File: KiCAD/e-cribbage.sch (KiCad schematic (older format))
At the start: 559 parts, among them U1 74HC595D_118, U10 74HC595D_118, U11 74HC595D_118, U12 74HC595D_118, U13 74HC595D_118, U14 74HC595D_118, U15 74HC595D_118, U16 74HC595D_118, U17 74HC595D_118, U18 74HC595D_118, U19 74HC595D_118, U2 MSP430F2012IPW, U20 74HC595D_118, U21 74HC595D_118, U22 74HC595D_118, U23 74HC595D_118, U24 74HC595D_118, U25 74HC595D_118, U26 74HC595D_118, U27 74HC595D_118, U28 74HC595D_118, U29 74HC595D_118, U3 74HC595D_118, U30 74HC595D_118, U31 74HC595D_118, U32 SN74LVC1G08DBVR, U33 SN74LVC1G125DCKR, U4 74HC595D_118, U5 74HC595D_118, U6 74HC595D_118, U7 74HC595D_118, U8 74HC595D_118, U9 74HC595D_118

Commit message: reduced 0603 footprints
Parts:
- D100, D101, D102, D103, D104, D105, D106, D107, D108, D109, D11, D110, D111, D112, D113, D114, D115, D116, D117, D118, D119, D12, D120, D121, D122, D123, D124, D125, D126, D127, D128, D129, D13, D130, D131, D132, D133, D134, D135, D136, D137, D138, D139, D14, D140, D141, D142, D143, D144, D145, D146, D147, D148, D149, D15, D150, D151, D152, D153, D154, D155, D156, D157, D158, D159, D16, D160, D161, D162, D163, D164, D165, D166, D167, D168, D169, D17, D170, D171, D172, D173, D174, D175, D176, D177, D178, D179, D18, D180, D181, D182, D183, D184, D185, D186, D187, D188, D189, D19, D190, D191, D192, D193, D194, D195, D196, D197, D198, D199, D20, D200, D201, D202, D203, D204, D205, D206, D207, D208, D209, D21, D210, D211, D212, D213, D214, D215, D216, D217, D218, D219, D22, D220, D221, D222, D223, D224, D225, D226, D227, D228, D229, D23, D230, D231, D232, D233, D234, D235, D236, D237, D238, D239, D24, D240, D25, D26, D27, D28, D29, D30, D31, D32, D33, D34, D35, D36, D37, D38, D39, D40, D41, D42, D43, D44, D45, D46, D47, D48, D49, D50, D51, D52, D53, D54, D55, D56, D57, D58, D59, D60, D61, D62, D63, D64, D65, D66, D67, D68, D69, D70, D71, D72, D73, D74, D75, D76, D77, D78, D79, D80, D81, D82, D83, D84, D85, D86, D87, D88, D89, D90, D91, D92, D93, D94, D95, D96, D97, D98, D99: footprint LEDs:LED_0603_HandSoldering -> LEDs:LED_0603
- R100, R101, R102, R103, R104, R105, R106, R107, R108, R109, R11, R110, R111, R112, R113, R114, R115, R116, R117, R118, R119, R12, R120, R121, R122, R123, R124, R125, R126, R127, R128, R129, R13, R130, R131, R132, R133, R134, R135, R136, R137, R138, R139, R14, R140, R141, R142, R143, R144, R145, R146, R147, R148, R149, R15, R150, R151, R152, R153, R154, R155, R156, R157, R158, R159, R16, R160, R161, R162, R163, R164, R165, R166, R167, R168, R169, R17, R170, R171, R172, R173, R174, R175, R176, R177, R178, R179, R18, R180, R181, R182, R183, R184, R185, R186, R187, R188, R189, R19, R190, R191, R192, R193, R194, R195, R196, R197, R198, R199, R20, R200, R201, R202, R203, R204, R205, R206, R207, R208, R209, R21, R210, R211, R212, R213, R214, R215, R216, R217, R218, R219, R22, R220, R221, R222, R223, R224, R225, R226, R227, R228, R229, R23, R230, R231, R232, R233, R234, R235, R236, R237, R238, R239, R24, R240, R241, R242, R243, R244, R245, R246, R247, R248, R249, R25, R250, R26, R27, R28, R29, R30, R31, R32, R33, R34, R35, R36, R37, R38, R39, R40, R41, R42, R43, R44, R45, R46, R47, R48, R49, R50, R51, R52, R53, R54, R55, R56, R57, R58, R59, R60, R61, R62, R63, R64, R65, R66, R67, R68, R69, R70, R71, R72, R73, R74, R75, R76, R77, R78, R79, R80, R81, R82, R83, R84, R85, R86, R87, R88, R89, R90, R91, R92, R93, R94, R95, R96, R97, R98, R99: footprint Resistors_SMD:R_0603_HandSoldering -> Resistors_SMD:R_0603

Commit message: power and ground planes added 471 nets unconnected
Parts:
- added C32, C33, C34, C35: 1.0uF, Capacitors_SMD:C_0603_HandSoldering, symbol Device:C
- added R251: 47k, Resistors_SMD:R_0603, symbol Device:R
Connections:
- net labels added: RST, TEST
- wire segments 1708 -> 1768
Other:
- moved on the sheet: BAT1, C2, R243, R244, R246, R247, S1, S2, S3, S4, U2

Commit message: preliminary part placement and route
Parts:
- removed R241, R242, R245, R248, R249, R250: 10k, Resistors_SMD:R_0603, symbol Device:R
- removed U33: SN74LVC1G125DCKR, digikey-footprints:SOT-353, symbol dk_Logic-Buffers-Drivers-Receivers-Transceivers:SN74LVC1G125DCKR
- added C36, C37, C38, C39: 1.0uF, Capacitors_SMD:C_0603_HandSoldering, symbol Device:C
- added U34, U35, U36, U37, U38, U39, U40: SN74LVC1G08DBVR, digikey-footprints:SOT-753, symbol dk_Logic-Gates-and-Inverters:SN74LVC1G08DBVR
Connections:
- net labels added: CLK1A, CLK1B, CLK1C, CLK1D, CLK2A, CLK2B, CLK2C, CLK2D
- wire segments 1768 -> 1848
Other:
- moved on the sheet: BAT1, C2, C32, C33, C34, C35, R243, R244, R246, R247, R251, S1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

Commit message: clock fanout added to schematic
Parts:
- BAT1: symbol dk_Battery-Holders-Clips-Contacts:BS-7 -> e-cribbage-rescue:BS-7-dk_Battery-Holders-Clips-Contacts
- S1, S2, S3, S4: symbol dk_Pushbutton-Switches:GPTS203211B -> e-cribbage-rescue:GPTS203211B-dk_Pushbutton-Switches
- U1, U10, U11, U12, U13, U14, U15, U16, U17, U18, U19, U20, U21, U22, U23, U24, U25, U26, U27, U28, U29, U3, U30, U31, U4, U5, U6, U7, U8, U9: symbol dk_Logic-Shift-Registers:74HC595D_118 -> e-cribbage-rescue:74HC595D_118-dk_Logic-Shift-Registers
- U32, U34, U35, U36, U37, U38, U39, U40: symbol dk_Logic-Gates-and-Inverters:SN74LVC1G08DBVR -> e-cribbage-rescue:SN74LVC1G08DBVR-dk_Logic-Gates-and-Inverters
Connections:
- net +3V3: now also U10.10 (MR), U10.13 (OE), U11.10 (MR), U11.13 (OE), U12.10 (MR), U12.13 (OE), U13.10 (MR), U13.13 (OE), U14.10 (MR), U14.13 (OE), U17.10 (MR), U17.13 (OE), U18.10 (MR), U18.13 (OE), U19.10 (MR), U19.13 (OE), U20.10 (MR), U20.13 (OE), U21.10 (MR), U21.13 (OE), U22.10 (MR), U22.13 (OE), U23.10 (MR), U23.13 (OE), U24.10 (MR), U24.13 (OE), U25.10 (MR), U25.13 (OE), U26.10 (MR), U26.13 (OE), U27.10 (MR), U27.13 (OE), U28.10 (MR), U28.13 (OE), U29.10 (MR), U29.13 (OE), U30.10 (MR), U30.13 (OE), U31.10 (MR), U31.13 (OE), U5.10 (MR), U5.13 (OE), U6.10 (MR), U6.13 (OE), U7.10 (MR), U7.13 (OE), U8.10 (MR), U8.13 (OE), U9.10 (MR), U9.13 (OE)
- net CLK: no longer U17.11 (SHCP), U17.12 (STCP)
- net CLK1B: now also U6.11 (SHCP), U6.12 (STCP), U7.11 (SHCP), U7.12 (STCP), U8.11 (SHCP), U8.12 (STCP), U9.11 (SHCP), U9.12 (STCP)
- net CLK1C: now also U10.11 (SHCP), U10.12 (STCP), U11.11 (SHCP), U11.12 (STCP), U12.11 (SHCP), U12.12 (STCP), U13.11 (SHCP), U13.12 (STCP)
- net CLK1D: now also U14.11 (SHCP), U14.12 (STCP), U15.11 (SHCP), U15.12 (STCP), U16.11 (SHCP), U16.12 (STCP)
- net CLK2A: now also U17.11 (SHCP), U17.12 (STCP), U18.11 (SHCP), U18.12 (STCP), U19.11 (SHCP), U19.12 (STCP), U20.11 (SHCP), U20.12 (STCP)
- net CLK2B: now also U21.11 (SHCP), U21.12 (STCP), U22.11 (SHCP), U22.12 (STCP), U23.11 (SHCP), U23.12 (STCP), U24.11 (SHCP), U24.12 (STCP)
- net CLK2C: now also U26.11 (SHCP), U26.12 (STCP), U27.11 (SHCP), U27.12 (STCP), U28.11 (SHCP), U28.12 (STCP)
- net CLK2D: now also U29.11 (SHCP), U29.12 (STCP), U30.11 (SHCP), U30.12 (STCP), U31.11 (SHCP), U31.12 (STCP)
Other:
- moved on the sheet: C17, C18, C19, C20, C21, C22, C29, C30, C31, D121, D122, D123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

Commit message: OE pulled low
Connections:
- net +3V3: no longer U1.13 (OE), U10.13 (OE), U11.13 (OE), U12.13 (OE), U13.13 (OE), U14.13 (OE), U15.13 (OE), U16.13 (OE), U17.13 (OE), U18.13 (OE), U19.13 (OE), U20.13 (OE), U21.13 (OE), U22.13 (OE), U25.13 (OE), U26.13 (OE), U27.13 (OE), U28.13 (OE), U29.13 (OE), U3.13 (OE), U30.13 (OE), U31.13 (OE), U5.13 (OE), U6.13 (OE), U7.13 (OE), U8.13 (OE), U9.13 (OE)
- net CLK2C: now also U25.11 (SHCP), U25.12 (STCP)
- net GND: now also U1.13 (OE), U10.13 (OE), U11.13 (OE), U12.13 (OE), U13.13 (OE), U14.13 (OE), U15.13 (OE), U16.13 (OE), U17.13 (OE), U18.13 (OE), U19.13 (OE), U20.13 (OE), U21.13 (OE), U22.13 (OE), U25.13 (OE), U26.13 (OE), U27.13 (OE), U28.13 (OE), U29.13 (OE), U3.13 (OE), U30.13 (OE), U31.13 (OE), U5.13 (OE), U6.13 (OE), U7.13 (OE), U8.13 (OE), U9.13 (OE)

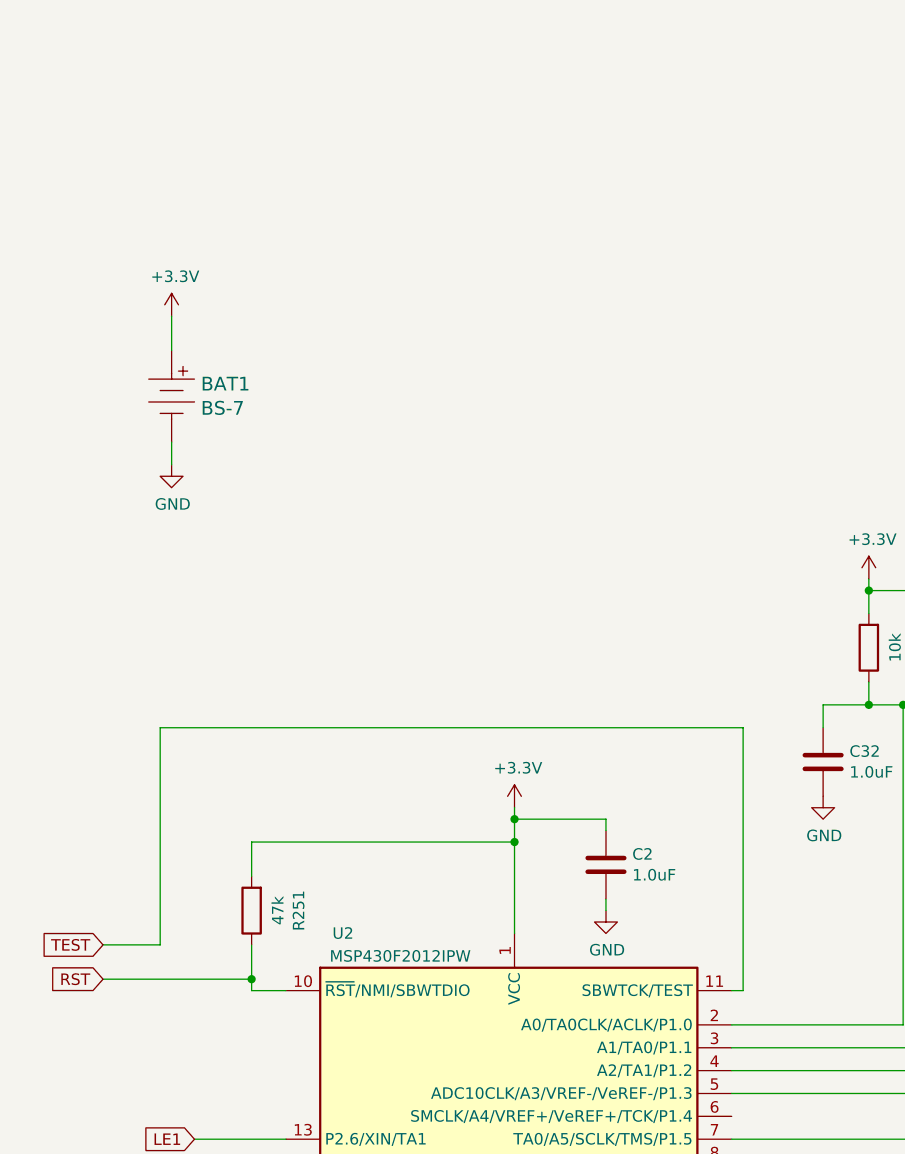
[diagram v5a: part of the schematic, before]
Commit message: added FET connector
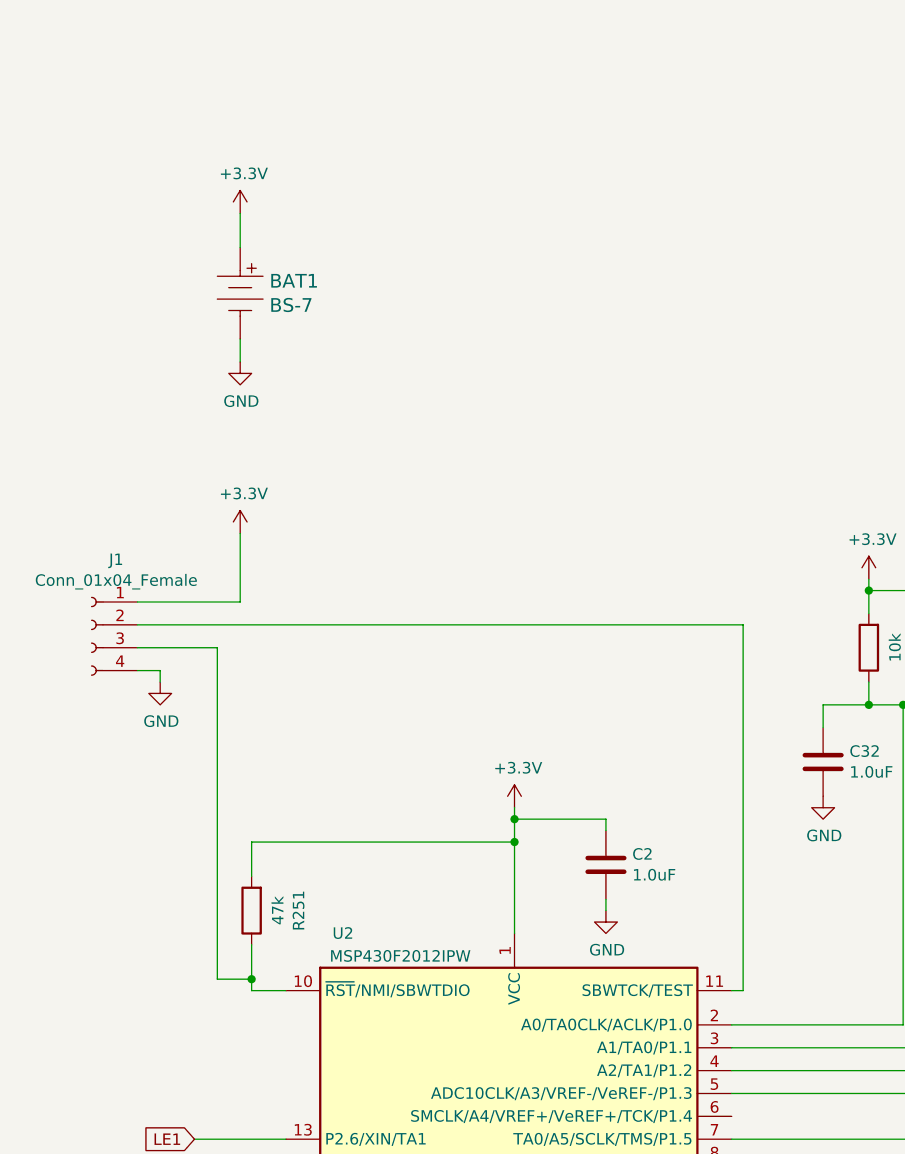
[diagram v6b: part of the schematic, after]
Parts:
- added J1: Conn_01x04_Female, Connector_PinHeader_1.27mm:PinHeader_1x04_P1.27mm_Vertical, symbol Connector:Conn_01x04_Female
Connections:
- net +3V3: now also J1.1 (Pin_1)
- net GND: now also J1.4 (Pin_4)
- net RST: no longer names the net of R251.1, U2.10 (~RST~/NMI/SBWTDIO)
- net RST: now also J1.3 (Pin_3)
- net TEST: no longer names the net of U2.11 (SBWTCK/TEST)
- net TEST: now also J1.2 (Pin_2)
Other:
- moved on the sheet: BAT1
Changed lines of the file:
@@
 L e-cribbage-rescue:BS-7-dk_Battery-Holders-Clips-Contacts BAT1
 U 1 1 6DDA013A
-P 1250 2850
-F 0 "BAT1" H 1378 2903 60  0000 L CNN
-F 1 "BS-7" H 1378 2797 60  0000 L CNN
-F 2 "Battery_Holders:Keystone_1058_1x2032-CoinCell" H 1450 3050 60  0001 L CNN
-F 3 "http://www.memoryprotectiondevices.com/datasheets/BS-7-datasheet.pdf" V 1450 3150 60  0001 L CNN
-F 4 "BS-7-ND" H 1450 3250 60  0001 L CNN "Digi-Key_PN"
-F 5 "BS-7" H 1450 3350 60  0001 L CNN "MPN"
-F 6 "Battery Products" H 1450 3450 60  0001 L CNN "Category"
-F 7 "Battery Holders, Clips, Contacts" H 1450 3550 60  0001 L CNN "Family"
-F 8 "http://www.memoryprotectiondevices.com/datasheets/BS-7-datasheet.pdf" H 1450 3650 60  0001 L CNN "DK_Datasheet_Link"
-F 9 "/product-detail/en/mpd-memory-protection-devices/BS-7/BS-7-ND/389447" H 1450 3750 60  0001 L CNN "DK_Detail_Page"
-F 10 "BATTERY HOLDER COIN 20MM PC PIN" H 1450 3850 60  0001 L CNN "Description"
-F 11 "MPD (Memory Protection Devices)" H 1450 3950 60  0001 L CNN "Manufacturer"
-F 12 "Active" H 1450 4050 60  0001 L CNN "Status"
-	1    1250 2850
+P 1550 2400
+F 0 "BAT1" H 1678 2453 60  0000 L CNN
+F 1 "BS-7" H 1678 2347 60  0000 L CNN
+F 2 "Battery_Holders:Keystone_1058_1x2032-CoinCell" H 1750 2600 60  0001 L CNN
+F 3 "http://www.memoryprotectiondevices.com/datasheets/BS-7-datasheet.pdf" V 1750 2700 60  0001 L CNN
+F 4 "BS-7-ND" H 1750 2800 60  0001 L CNN "Digi-Key_PN"
+F 5 "BS-7" H 1750 2900 60  0001 L CNN "MPN"
+F 6 "Battery Products" H 1750 3000 60  0001 L CNN "Category"
+F 7 "Battery Holders, Clips, Contacts" H 1750 3100 60  0001 L CNN "Family"
+F 8 "http://www.memoryprotectiondevices.com/datasheets/BS-7-datasheet.pdf" H 1750 3200 60  0001 L CNN "DK_Datasheet_Link"
+F 9 "/product-detail/en/mpd-memory-protection-devices/BS-7/BS-7-ND/389447" H 1750 3300 60  0001 L CNN "DK_Detail_Page"
+F 10 "BATTERY HOLDER COIN 20MM PC PIN" H 1750 3400 60  0001 L CNN "Description"
+F 11 "MPD (Memory Protection Devices)" H 1750 3500 60  0001 L CNN "Manufacturer"
+F 12 "Active" H 1750 3600 60  0001 L CNN "Status"
+	1    1550 2400
 	1    0    0    -1
 $EndComp
@@
 L power:GND #PWR0334
 U 1 1 6DDA1AA0
-P 1250 3150
-F 0 "#PWR0334" H 1250 2900 50  0001 C CNN
-F 1 "GND" H 1255 2977 50  0000 C CNN
-F 2 "" H 1250 3150 50  0001 C CNN
-F 3 "" H 1250 3150 50  0001 C CNN
-	1    1250 3150
+P 1550 2700
+F 0 "#PWR0334" H 1550 2450 50  0001 C CNN
+F 1 "GND" H 1555 2527 50  0000 C CNN
+F 2 "" H 1550 2700 50  0001 C CNN
+F 3 "" H 1550 2700 50  0001 C CNN
+	1    1550 2700
 	1    0    0    -1
 $EndComp
@@
 L power:+3.3V #PWR0335
 U 1 1 6DDA1D80
-P 1250 2500
-F 0 "#PWR0335" H 1250 2350 50  0001 C CNN
-F 1 "+3.3V" H 1265 2673 50  0000 C CNN
-F 2 "" H 1250 2500 50  0001 C CNN
-F 3 "" H 1250 2500 50  0001 C CNN
-	1    1250 2500
-	1    0    0    -1
-$EndComp
-Wire Wire Line
-	1250 2500 1250 2650
-Wire Wire Line
-	1250 3050 1250 3150
+P 1550 2050
+F 0 "#PWR0335" H 1550 1900 50  0001 C CNN
+F 1 "+3.3V" H 1565 2223 50  0000 C CNN
+F 2 "" H 1550 2050 50  0001 C CNN
+F 3 "" H 1550 2050 50  0001 C CNN
+	1    1550 2050
+	1    0    0    -1
+$EndComp
+Wire Wire Line
+	1550 2050 1550 2200
+Wire Wire Line
+	1550 2600 1550 2700
 $Comp
 L power:GND #PWR0341
@@
 Wire Wire Line
 	2750 4800 2750 5200
-Text GLabel 950  5400 0    50   Input ~ 0
-RST
-Text GLabel 950  5250 0    50   Input ~ 0
-TEST
-Wire Wire Line
-	950  5250 1200 5250
-Wire Wire Line
-	1200 5250 1200 4300
-Wire Wire Line
-	1200 4300 3750 4300
 Wire Wire Line
 	3750 5450 3700 5450
 Wire Wire Line
-	950  5400 1600 5400
+	1450 5400 1600 5400
 Connection ~ 1600 5400
 Wire Wire Line
@@
 	4100 4200 4300 4200
 Wire Wire Line
-	3750 4300 3750 5450
+	3750 3850 3750 5450
 $Comp
 L e-cribbage-rescue:SN74LVC1G08DBVR-dk_Logic-Gates-and-Inverters U34
@@
 Wire Wire Line
 	30050 8750 30050 8850
+$Comp
+L Connector:Conn_01x04_Female J1
+U 1 1 5F480BDE
+P 900 3850
+F 0 "J1" H 792 4135 50  0000 C CNN
+F 1 "Conn_01x04_Female" H 792 4044 50  0000 C CNN
+F 2 "Connector_PinHeader_1.27mm:PinHeader_1x04_P1.27mm_Vertical" H 900 3850 50  0001 C CNN
+F 3 "~" H 900 3850 50  0001 C CNN
+	1    900  3850
+	-1   0    0    -1
+$EndComp
+$Comp
+L power:+3.3V #PWR0362
+U 1 1 5F940DFF
+P 1550 3450
+F 0 "#PWR0362" H 1550 3300 50  0001 C CNN
+F 1 "+3.3V" H 1565 3623 50  0000 C CNN
+F 2 "" H 1550 3450 50  0001 C CNN
+F 3 "" H 1550 3450 50  0001 C CNN
+	1    1550 3450
+	1    0    0    -1
+$EndComp
+Wire Wire Line
+	1100 3750 1550 3750
+Wire Wire Line
+	1550 3750 1550 3450
+$Comp
+L power:GND #PWR0363
+U 1 1 5FDFA229
+P 1200 4100
+F 0 "#PWR0363" H 1200 3850 50  0001 C CNN
+F 1 "GND" H 1205 3927 50  0000 C CNN
+F 2 "" H 1200 4100 50  0001 C CNN
+F 3 "" H 1200 4100 50  0001 C CNN
+	1    1200 4100
+	1    0    0    -1
+$EndComp
+Wire Wire Line
+	1200 4100 1200 4050
+Wire Wire Line
+	1200 4050 1100 4050
+Wire Wire Line
+	1100 3850 3750 3850
+Wire Wire Line
+	1450 5400 1450 3950
+Wire Wire Line
+	1450 3950 1100 3950
 $EndSCHEMATC

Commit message: created local library
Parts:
- D1, D10, D100, D101, D102, D103, D104, D105, D106, D107, D108, D109, D11, D110, D111, D112, D113, D114, D115, D116, D117, D118, D119, D12, D120, D121, D122, D123, D124, D125, D126, D127, D128, D129, D13, D130, D131, D132, D133, D134, D135, D136, D137, D138, D139, D14, D140, D141, D142, D143, D144, D145, D146, D147, D148, D149, D15, D150, D151, D152, D153, D154, D155, D156, D157, D158, D159, D16, D160, D161, D162, D163, D164, D165, D166, D167, D168, D169, D17, D170, D171, D172, D173, D174, D175, D176, D177, D178, D179, D18, D180, D181, D182, D183, D184, D185, D186, D187, D188, D189, D19, D190, D191, D192, D193, D194, D195, D196, D197, D198, D199, D2, D20, D200, D201, D202, D203, D204, D205, D206, D207, D208, D209, D21, D210, D211, D212, D213, D214, D215, D216, D217, D218, D219, D22, D220, D221, D222, D223, D224, D225, D226, D227, D228, D229, D23, D230, D231, D232, D233, D234, D235, D236, D237, D238, D239, D24, D240, D25, D26, D27, D28, D29, D3, D30, D31, D32, D33, D34, D35, D36, D37, D38, D39, D4, D40, D41, D42, D43, D44, D45, D46, D47, D48, D49, D5, D50, D51, D52, D53, D54, D55, D56, D57, D58, D59, D6, D60, D61, D62, D63, D64, D65, D66, D67, D68, D69, D7, D70, D71, D72, D73, D74, D75, D76, D77, D78, D79, D8, D80, D81, D82, D83, D84, D85, D86, D87, D88, D89, D9, D90, D91, D92, D93, D94, D95, D96, D97, D98, D99: footprint LEDs:LED_0603 -> e-cribbage:LED_0603
- R1, R10, R100, R101, R102, R103, R104, R105, R106, R107, R108, R109, R11, R110, R111, R112, R113, R114, R115, R116, R117, R118, R119, R12, R120, R121, R122, R123, R124, R125, R126, R127, R128, R129, R13, R130, R131, R132, R133, R134, R135, R136, R137, R138, R139, R14, R140, R141, R142, R143, R144, R145, R146, R147, R148, R149, R15, R150, R151, R152, R153, R154, R155, R156, R157, R158, R159, R16, R160, R161, R162, R163, R164, R165, R166, R167, R168, R169, R17, R170, R171, R172, R173, R174, R175, R176, R177, R178, R179, R18, R180, R181, R182, R183, R184, R185, R186, R187, R188, R189, R19, R190, R191, R192, R193, R194, R195, R196, R197, R198, R199, R2, R20, R200, R201, R202, R203, R204, R205, R206, R207, R208, R209, R21, R210, R211, R212, R213, R214, R215, R216, R217, R218, R219, R22, R220, R221, R222, R223, R224, R225, R226, R227, R228, R229, R23, R230, R231, R232, R233, R234, R235, R236, R237, R238, R239, R24, R240, R243, R244, R246, R247, R25, R251, R26, R27, R28, R29, R3, R30, R31, R32, R33, R34, R35, R36, R37, R38, R39, R4, R40, R41, R42, R43, R44, R45, R46, R47, R48, R49, R5, R50, R51, R52, R53, R54, R55, R56, R57, R58, R59, R6, R60, R61, R62, R63, R64, R65, R66, R67, R68, R69, R7, R70, R71, R72, R73, R74, R75, R76, R77, R78, R79, R8, R80, R81, R82, R83, R84, R85, R86, R87, R88, R89, R9, R90, R91, R92, R93, R94, R95, R96, R97, R98, R99: footprint Resistors_SMD:R_0603 -> e-cribbage:R_0603

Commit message: schematic fixes + routes + battery clip
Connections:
- net +3V3: no longer U23.13 (OE), U24.13 (OE), U4.13 (OE)
- net GND: now also U23.13 (OE), U24.13 (OE), U4.13 (OE)
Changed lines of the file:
@@
 $EndComp
 Wire Wire Line
-	7550 9200 7550 9350
+	7550 9200 7550 9250
 $Comp
 L power:+3.3V #PWR026
@@
 $EndComp
 Wire Wire Line
-	25450 2950 25450 3100
+	25450 2950 25450 3050
 $Comp
 L power:+3.3V #PWR0235
@@
 $EndComp
 Wire Wire Line
-	25400 5900 25400 6050
+	25400 5900 25400 5950
 $Comp
 L power:+3.3V #PWR0245
@@
 	7150 8700 7000 8700
 Wire Wire Line
-	7000 8700 7000 8400
-Wire Wire Line
 	7000 8400 7050 8400
 Wire Wire Line
@@
 	25050 2450 24750 2450
 Wire Wire Line
-	24750 2450 24750 2150
-Wire Wire Line
 	24750 1650 25450 1650
 Connection ~ 25450 1650
@@
 Wire Wire Line
 	25050 2150 24750 2150
-Connection ~ 24750 2150
 Wire Wire Line
 	24750 2150 24750 1650
@@
 	25000 5400 24700 5400
 Wire Wire Line
-	24700 5400 24700 5100
-Wire Wire Line
 	24700 4450 25400 4450
 Connection ~ 25400 4450
@@
 Wire Wire Line
 	25000 5100 24700 5100
-Connection ~ 24700 5100
 Wire Wire Line
 	24700 5100 24700 4450
@@
 Wire Wire Line
 	1450 3950 1100 3950
+Wire Wire Line
+	7000 8700 7000 9250
+Wire Wire Line
+	7000 9250 7550 9250
+Connection ~ 7550 9250
+Wire Wire Line
+	7550 9250 7550 9350
+Wire Wire Line
+	24750 2450 24750 3050
+Wire Wire Line
+	24750 3050 25450 3050
+Connection ~ 25450 3050
+Wire Wire Line
+	25450 3050 25450 3100
+Wire Wire Line
+	24700 5400 24700 5950
+Wire Wire Line
+	24700 5950 25400 5950
+Connection ~ 25400 5950
+Wire Wire Line
+	25400 5950 25400 6050
 $EndSCHEMATC
